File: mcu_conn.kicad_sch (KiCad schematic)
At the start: 38 parts, among them J11 MD_MCU_PU_EN, J9 MD_MCU_EN, Q6 FDV305N, U2 Teensy4.1, U3 INA190A5IDDFR, U4 INA190A5IDDFR

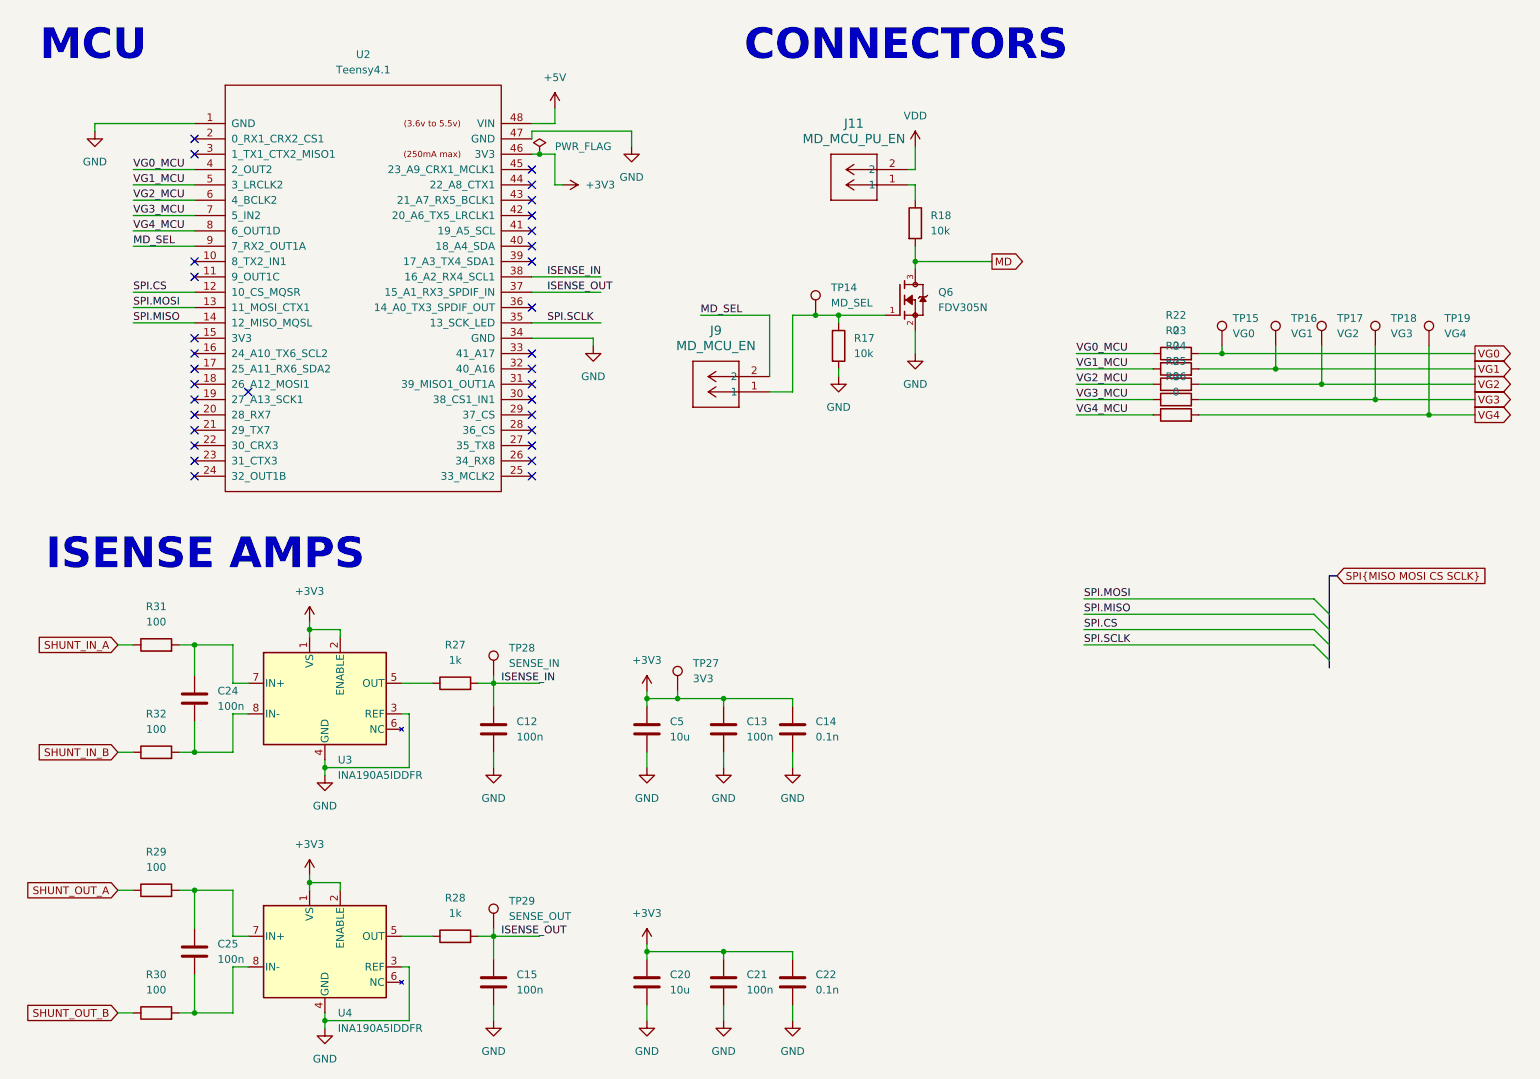
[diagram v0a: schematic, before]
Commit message: Monitor VDD, VDD_LDO, VOUT_LDO and VOUT on Teensy ADC pins through 10k
R45 to R48 connect Teensy pins 20, 19, 18 and 17 (A6, A5, A4, A3) to the
four rail nets. The 10k limits current if the Teensy is unpowered while
the chip is on. NR, IBIAS and MD stay off the Teensy.
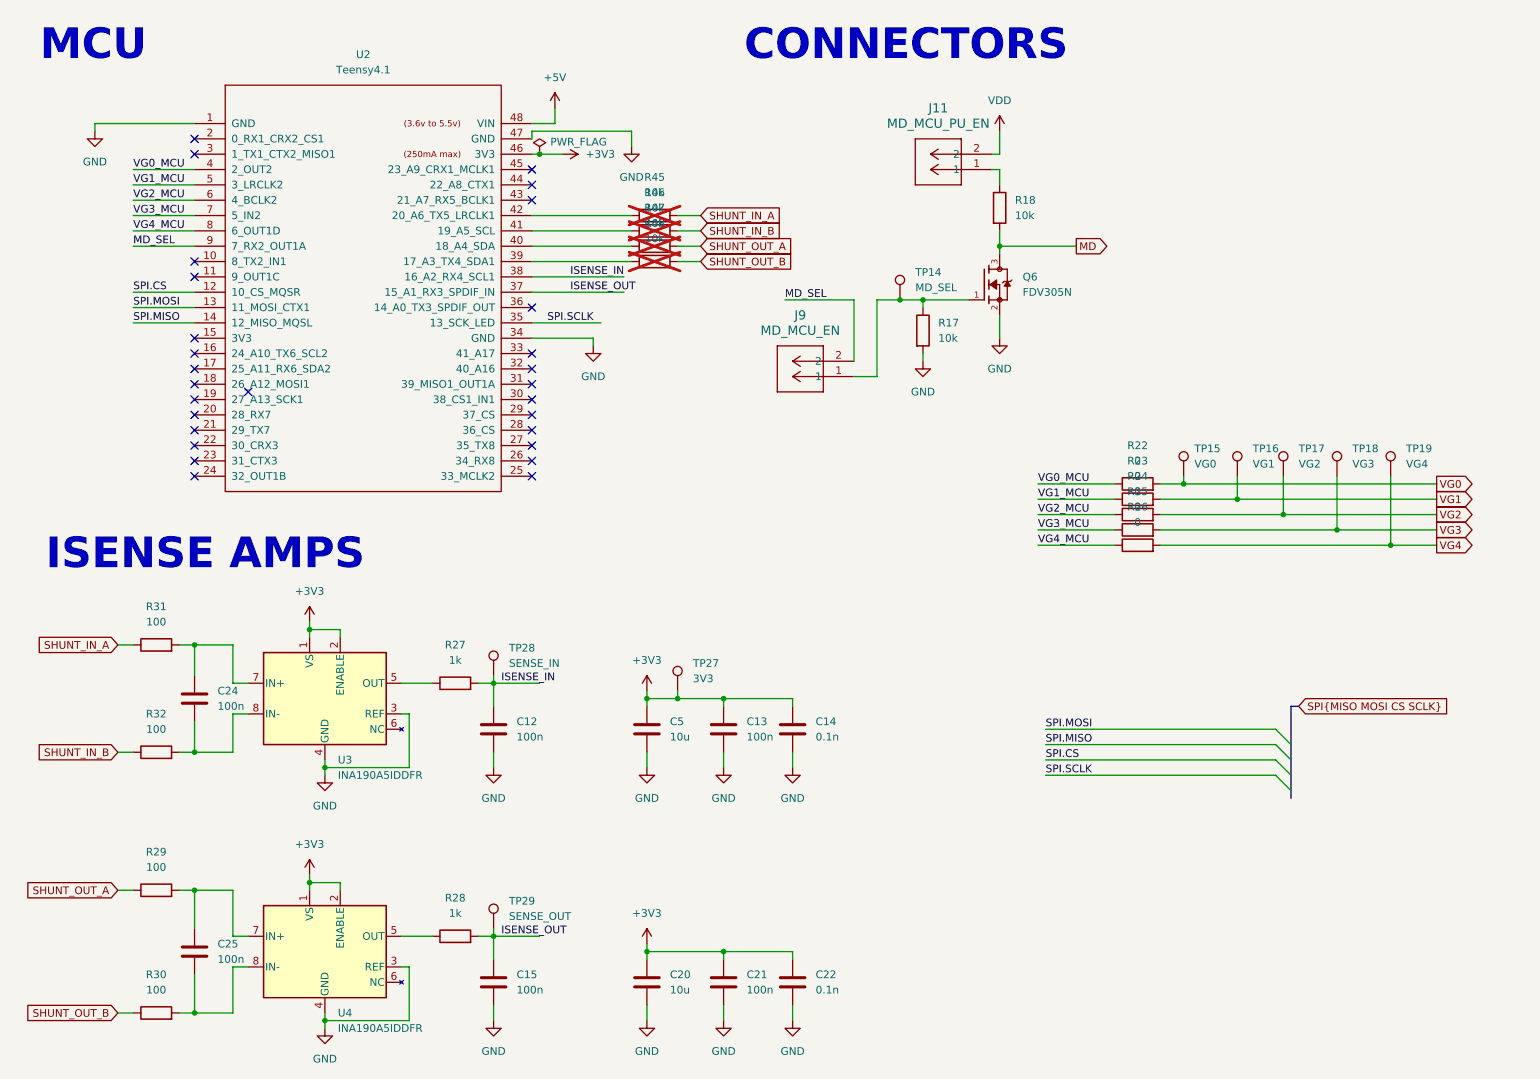
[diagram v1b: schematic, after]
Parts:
- added R45, R46, R47, R48: 10k, Resistor_SMD:R_0805_2012Metric_Pad1.20x1.40mm_HandSolder, symbol Device:R
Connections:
- net SHUNT_IN_A: now also R45.2
- net SHUNT_IN_B: now also R46.2
- net SHUNT_OUT_A: now also R47.2
- net SHUNT_OUT_B: now also R48.2
- net at U2.39 (17_A3_TX4_SDA1): now also R48.1
- net at U2.40 (18_A4_SDA): now also R47.1
- net at U2.41 (19_A5_SCL): now also R46.1
- net at U2.42 (20_A6_TX5_LRCLK1): now also R45.1
- no-connect marks 32 -> 28
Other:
- moved on the sheet: J11, J9, Q6, R17, R18, R22, R23, R24, R25, R26, TP14, TP15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

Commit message: Standardized resistor footprints
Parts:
- R17, R18, R22, R23, R24, R25, R26, R27, R28, R29, R30, R31, R32: footprint Resistor_SMD:R_0805_2012Metric_Pad1.20x1.40mm_HandSolder -> Resistor_SMD:R_0603_1608Metric_Pad0.98x0.95mm_HandSolder
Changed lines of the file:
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@@
 			)
 		)
-		(property "Footprint" "Resistor_SMD:R_0805_2012Metric_Pad1.20x1.40mm_HandSolder"
+		(property "Footprint" "Resistor_SMD:R_0603_1608Metric_Pad0.98x0.95mm_HandSolder"
 			(at 91.44 131.318 90)
 			(hide yes)
@@
 			)
 		)
-		(property "Footprint" "Resistor_SMD:R_0805_2012Metric_Pad1.20x1.40mm_HandSolder"
+		(property "Footprint" "Resistor_SMD:R_0603_1608Metric_Pad0.98x0.95mm_HandSolder"
 			(at 204.47 100.838 90)
 			(hide yes)
@@
 			)
 		)
-		(property "Footprint" "Resistor_SMD:R_0805_2012Metric_Pad1.20x1.40mm_HandSolder"
+		(property "Footprint" "Resistor_SMD:R_0603_1608Metric_Pad0.98x0.95mm_HandSolder"
 			(at 204.47 98.298 90)
 			(hide yes)
@@
 			)
 		)
-		(property "Footprint" "Resistor_SMD:R_0805_2012Metric_Pad1.20x1.40mm_HandSolder"
+		(property "Footprint" "Resistor_SMD:R_0603_1608Metric_Pad0.98x0.95mm_HandSolder"
 			(at 41.91 142.748 90)
 			(hide yes)
@@
 			)
 		)
-		(property "Footprint" "Resistor_SMD:R_0805_2012Metric_Pad1.20x1.40mm_HandSolder"
+		(property "Footprint" "Resistor_SMD:R_0603_1608Metric_Pad0.98x0.95mm_HandSolder"
 			(at 204.47 108.458 90)
 			(hide yes)
@@
 			)
 		)
-		(property "Footprint" "Resistor_SMD:R_0805_2012Metric_Pad1.20x1.40mm_HandSolder"
+		(property "Footprint" "Resistor_SMD:R_0603_1608Metric_Pad0.98x0.95mm_HandSolder"
 			(at 204.47 105.918 90)
 			(hide yes)
@@
 			)
 		)
-		(property "Footprint" "Resistor_SMD:R_0805_2012Metric_Pad1.20x1.40mm_HandSolder"
+		(property "Footprint" "Resistor_SMD:R_0603_1608Metric_Pad0.98x0.95mm_HandSolder"
 			(at 41.91 165.608 90)
 			(hide yes)
@@
 			)
 		)
-		(property "Footprint" "Resistor_SMD:R_0805_2012Metric_Pad1.20x1.40mm_HandSolder"
+		(property "Footprint" "Resistor_SMD:R_0603_1608Metric_Pad0.98x0.95mm_HandSolder"
 			(at 204.47 103.378 90)
 			(hide yes)
@@
 			)
 		)
-		(property "Footprint" "Resistor_SMD:R_0805_2012Metric_Pad1.20x1.40mm_HandSolder"
+		(property "Footprint" "Resistor_SMD:R_0603_1608Metric_Pad0.98x0.95mm_HandSolder"
 			(at 167.132 71.12 90)
 			(hide yes)
@@
 			)
 		)
-		(property "Footprint" "Resistor_SMD:R_0805_2012Metric_Pad1.20x1.40mm_HandSolder"
+		(property "Footprint" "Resistor_SMD:R_0603_1608Metric_Pad0.98x0.95mm_HandSolder"
 			(at 41.91 124.968 90)
 			(hide yes)
@@
 			)
 		)
-		(property "Footprint" "Resistor_SMD:R_0805_2012Metric_Pad1.20x1.40mm_HandSolder"
+		(property "Footprint" "Resistor_SMD:R_0603_1608Metric_Pad0.98x0.95mm_HandSolder"
 			(at 179.832 50.8 90)
 			(hide yes)
@@
 			)
 		)
-		(property "Footprint" "Resistor_SMD:R_0805_2012Metric_Pad1.20x1.40mm_HandSolder"
+		(property "Footprint" "Resistor_SMD:R_0603_1608Metric_Pad0.98x0.95mm_HandSolder"
 			(at 91.44 173.228 90)
 			(hide yes)
@@
 			)
 		)
-		(property "Footprint" "Resistor_SMD:R_0805_2012Metric_Pad1.20x1.40mm_HandSolder"
+		(property "Footprint" "Resistor_SMD:R_0603_1608Metric_Pad0.98x0.95mm_HandSolder"
 			(at 41.91 185.928 90)
 			(hide yes)
